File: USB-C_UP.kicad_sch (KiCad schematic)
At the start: 0 parts

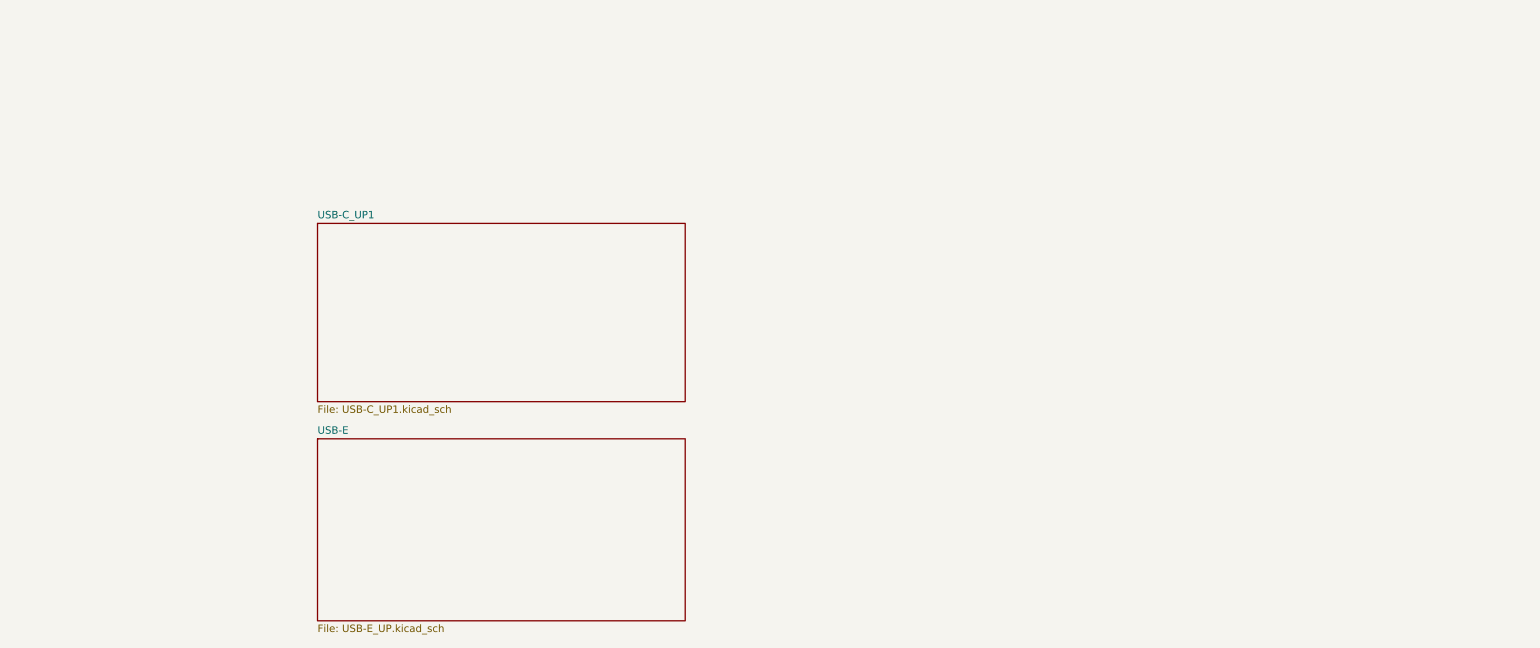
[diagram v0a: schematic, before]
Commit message: labels naming fixes, USB Type E connector added
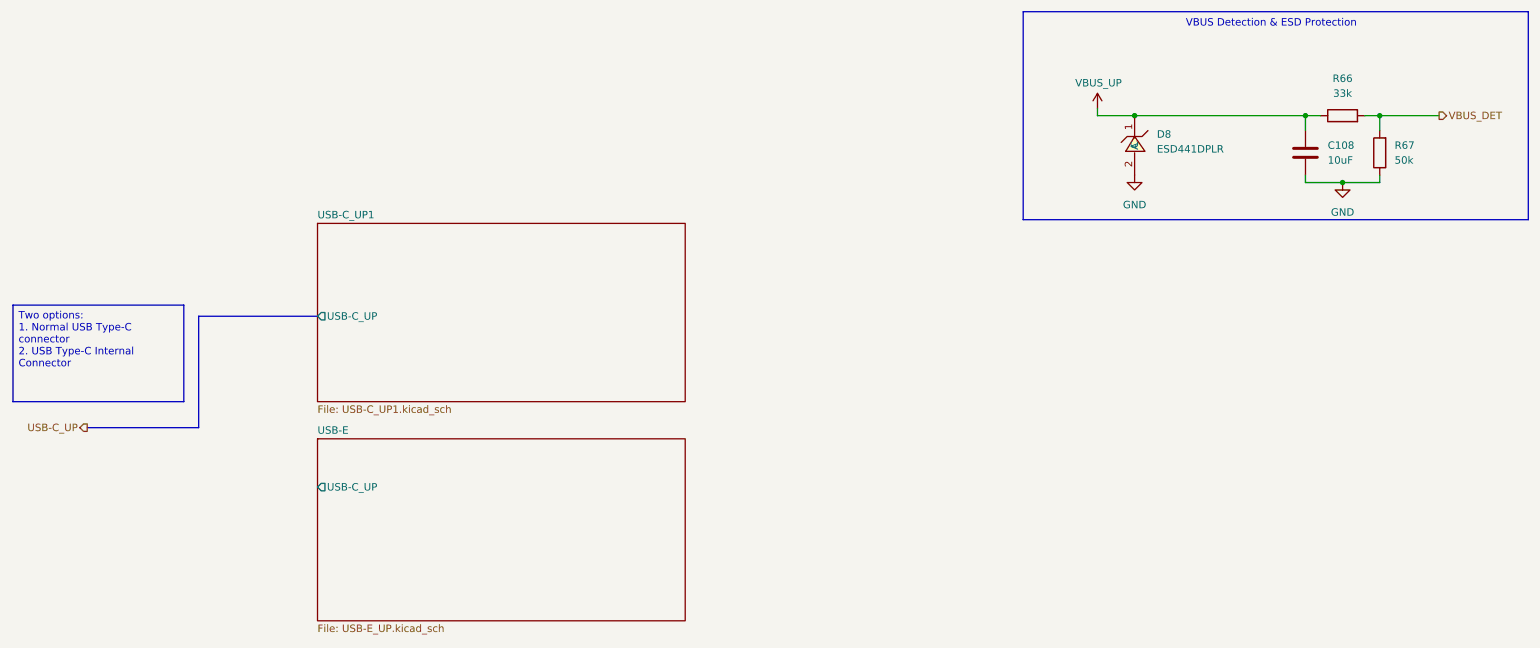
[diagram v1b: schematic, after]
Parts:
- added C108: 10uF, symbol Device:C
- added D8: ESD441DPLR, EasyEDA:X2SON-2_L0.6-W0.3-P0.35, symbol EasyEDA:ESD441DPLR
- added R66: 33k, symbol Device:R
- added R67: 50k, symbol Device:R
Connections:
- new net GND: C108.2, D8.2 (A), R67.1
- new net VBUS_DET: R66.2, R67.2
- new net VBUS_UP: C108.1, D8.1 (C), R66.1
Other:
- sheet USB-C_UP1 ports: added USB-C_UP; removed none
- sheet USB-E ports: added USB-C_UP; removed none
- note added: "VBUS Detection & ESD Protection"

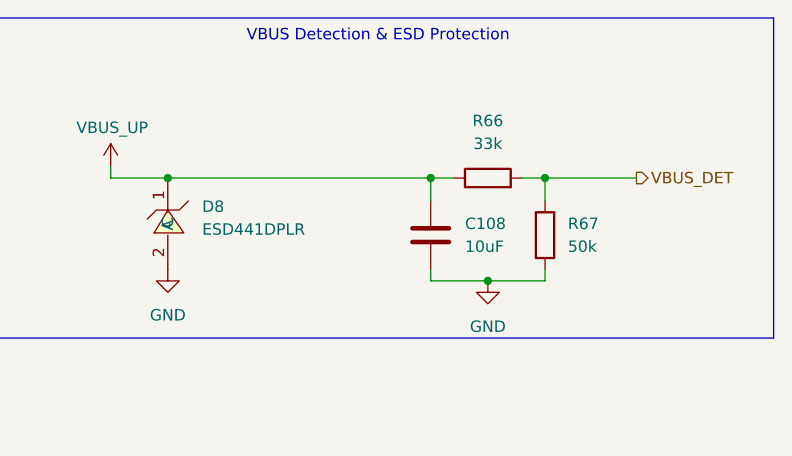
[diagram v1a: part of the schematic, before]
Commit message: TPS25762 EEPROM connector added
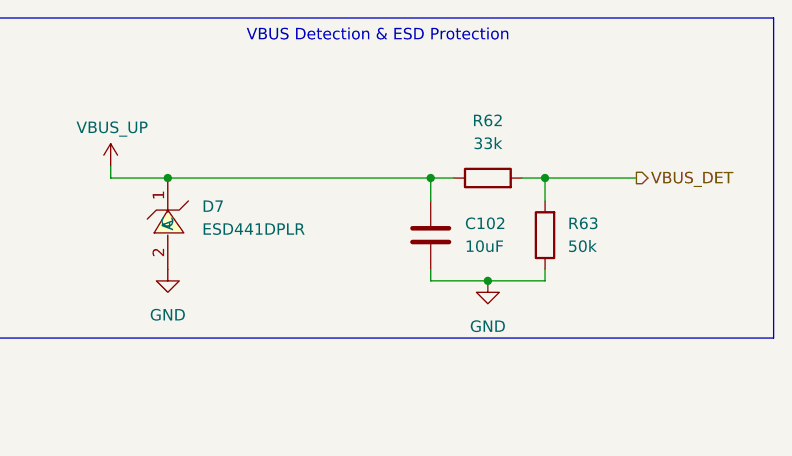
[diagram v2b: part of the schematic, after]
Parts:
- renumbered C108 to C102, D8 to D7, R66 to R62, R67 to R63
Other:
- title: (none) -> USB Hub
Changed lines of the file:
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@@
 	(generator_version "9.0")
 	(paper "A4")
+	(title_block
+		(title "USB Hub")
+	)
 	(rectangle
 		(start 191.77 17.78)
@@
 		(on_board yes)
 		(dnp no)
-		(property "Reference" "#PWR0199"
+		(property "Reference" "#PWR0186"
 			(at 204.47 38.1 0)
 			(effects
@@
 			(project "USB_hub"
 				(path "/a2586c28-95f1-49e6-9254-37d7a8473e53/7fe2d266-53fd-4db0-a3a6-d5a75d461820"
-					(reference "#PWR0199")
+					(reference "#PWR0186")
 					(unit 1)
 				)
@@
 		(dnp no)
 		(fields_autoplaced yes)
-		(property "Reference" "R66"
+		(property "Reference" "R62"
 			(at 246.38 29.21 90)
 			(effects
@@
 			(project "USB_hub"
 				(path "/a2586c28-95f1-49e6-9254-37d7a8473e53/7fe2d266-53fd-4db0-a3a6-d5a75d461820"
-					(reference "R66")
+					(reference "R62")
 					(unit 1)
 				)
@@
 		(dnp no)
 		(fields_autoplaced yes)
-		(property "Reference" "D8"
+		(property "Reference" "D7"
 			(at 214.63 38.7349 90)
 			(effects
@@
 			(project "USB_hub"
 				(path "/a2586c28-95f1-49e6-9254-37d7a8473e53/7fe2d266-53fd-4db0-a3a6-d5a75d461820"
-					(reference "D8")
+					(reference "D7")
 					(unit 1)
 				)
@@
 		(dnp no)
 		(fields_autoplaced yes)
-		(property "Reference" "#PWR0200"
+		(property "Reference" "#PWR0188"
 			(at 246.38 53.34 0)
 			(effects
@@
 			(project "USB_hub"
 				(path "/a2586c28-95f1-49e6-9254-37d7a8473e53/7fe2d266-53fd-4db0-a3a6-d5a75d461820"
-					(reference "#PWR0200")
+					(reference "#PWR0188")
 					(unit 1)
 				)
@@
 		(dnp no)
 		(fields_autoplaced yes)
-		(property "Reference" "#PWR0210"
+		(property "Reference" "#PWR0187"
 			(at 210.82 52.07 0)
 			(effects
@@
 			(project "USB_hub"
 				(path "/a2586c28-95f1-49e6-9254-37d7a8473e53/7fe2d266-53fd-4db0-a3a6-d5a75d461820"
-					(reference "#PWR0210")
+					(reference "#PWR0187")
 					(unit 1)
 				)
@@
 		(dnp no)
 		(fields_autoplaced yes)
-		(property "Reference" "C108"
+		(property "Reference" "C102"
 			(at 243.84 40.6399 0)
 			(effects
@@
 			(project "USB_hub"
 				(path "/a2586c28-95f1-49e6-9254-37d7a8473e53/7fe2d266-53fd-4db0-a3a6-d5a75d461820"
-					(reference "C108")
+					(reference "C102")
 					(unit 1)
 				)
@@
 		(dnp no)
 		(fields_autoplaced yes)
-		(property "Reference" "R67"
+		(property "Reference" "R63"
 			(at 255.27 40.6399 0)
 			(effects
@@
 			(project "USB_hub"
 				(path "/a2586c28-95f1-49e6-9254-37d7a8473e53/7fe2d266-53fd-4db0-a3a6-d5a75d461820"
-					(reference "R67")
+					(reference "R63")
 					(unit 1)
 				)

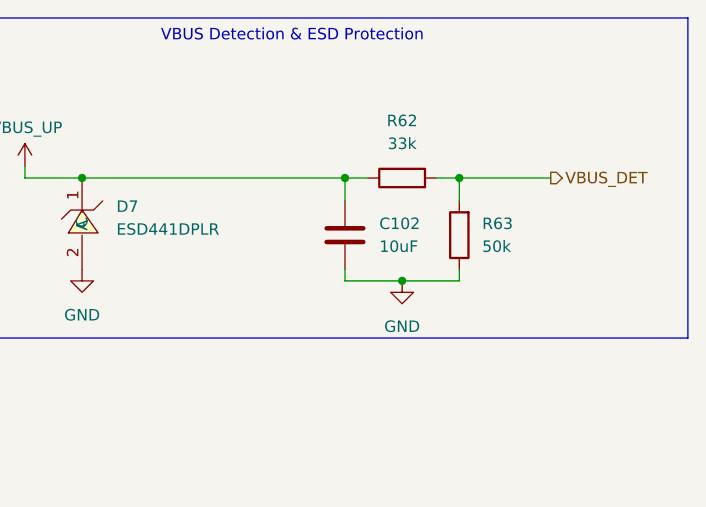
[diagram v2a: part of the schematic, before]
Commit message: deleted duplicated capacitor
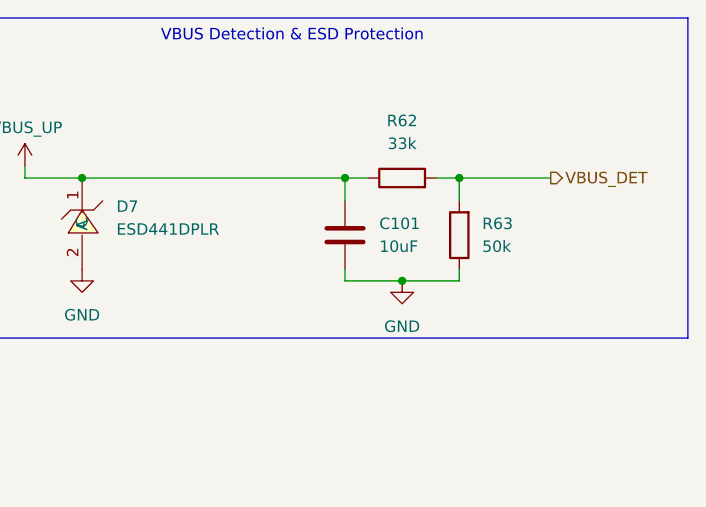
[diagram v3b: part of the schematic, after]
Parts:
- C101: renamed from C102; footprint (none) -> Capacitor_SMD:C_0402_1005Metric
- R62, R63: footprint (none) -> Resistor_SMD:R_0603_1608Metric
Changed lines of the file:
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@@
 			)
 		)
-		(property "Footprint" ""
+		(property "Footprint" "Resistor_SMD:R_0603_1608Metric"
 			(at 246.38 37.338 90)
 			(effects
@@
 		(dnp no)
 		(fields_autoplaced yes)
-		(property "Reference" "C102"
+		(property "Reference" "C101"
 			(at 243.84 40.6399 0)
 			(effects
@@
 			)
 		)
-		(property "Footprint" ""
+		(property "Footprint" "Capacitor_SMD:C_0402_1005Metric"
 			(at 240.9952 45.72 0)
 			(effects
@@
 			(project "USB_hub"
 				(path "/a2586c28-95f1-49e6-9254-37d7a8473e53/7fe2d266-53fd-4db0-a3a6-d5a75d461820"
-					(reference "C102")
+					(reference "C101")
 					(unit 1)
 				)
@@
 			)
 		)
-		(property "Footprint" ""
+		(property "Footprint" "Resistor_SMD:R_0603_1608Metric"
 			(at 254.508 41.91 90)
 			(effects

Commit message: Minor fixes
Fixed unclear labelling of buses
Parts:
- R62, R63: footprint Resistor_SMD:R_0603_1608Metric -> Resistor_SMD:R_0402_1005Metric
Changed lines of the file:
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@@
 			)
 		)
-		(property "Footprint" "Resistor_SMD:R_0603_1608Metric"
+		(property "Footprint" "Resistor_SMD:R_0402_1005Metric"
 			(at 246.38 37.338 90)
 			(effects
@@
 			)
 		)
-		(property "Footprint" "Resistor_SMD:R_0603_1608Metric"
+		(property "Footprint" "Resistor_SMD:R_0402_1005Metric"
 			(at 254.508 41.91 90)
 			(effects

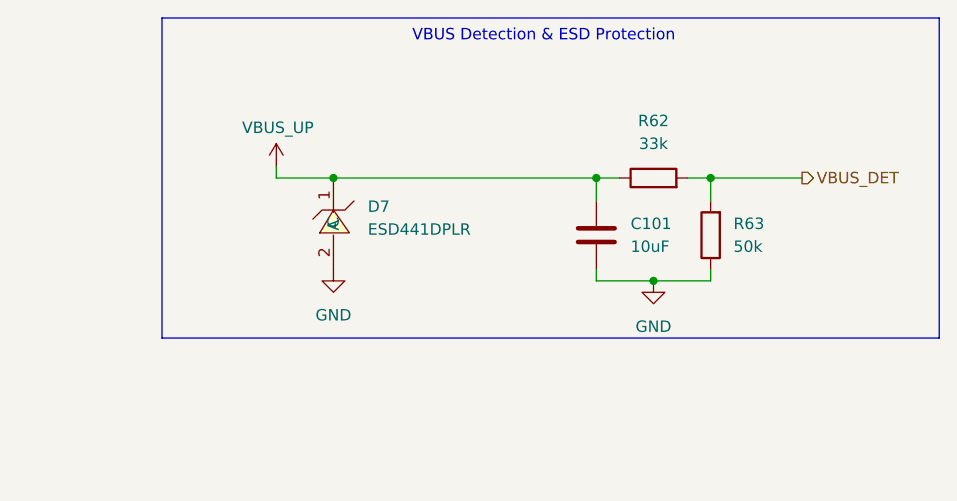
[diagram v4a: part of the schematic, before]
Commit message: MCP19035 changed to MP8795
TPS7A4701xRGW to AP7361C-33E
Led Indicator added
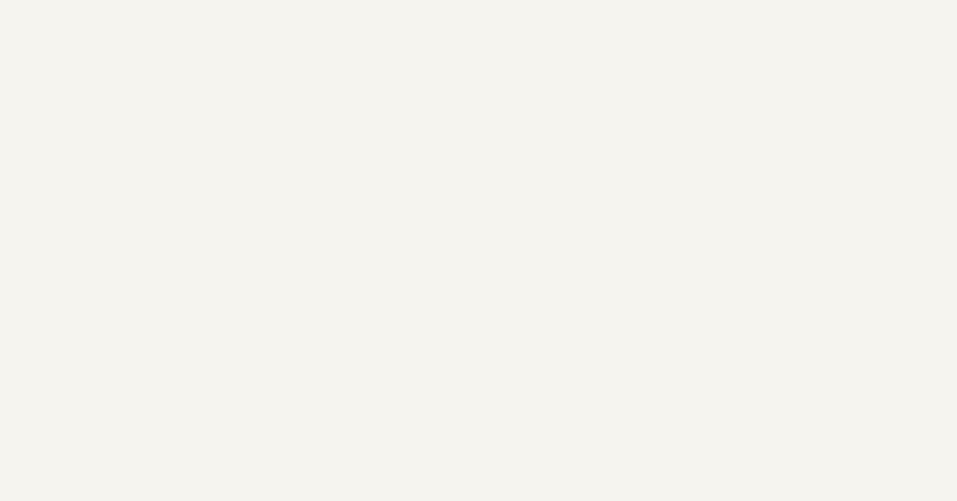
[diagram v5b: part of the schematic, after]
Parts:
- removed C101: 10uF, Capacitor_SMD:C_0402_1005Metric, symbol Device:C
- removed D7: ESD441DPLR, EasyEDA:X2SON-2_L0.6-W0.3-P0.35, symbol EasyEDA:ESD441DPLR
- removed R62: 33k, Resistor_SMD:R_0402_1005Metric, symbol Device:R
- removed R63: 50k, Resistor_SMD:R_0402_1005Metric, symbol Device:R
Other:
- note removed: "VBUS Detection & ESD Protection"
